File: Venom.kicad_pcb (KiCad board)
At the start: 2 copper layers, 72 x 42 mm, 13 parts, among them CN1 HC-XH-5A-G, CN2 HC-PH-8A-G, CN3 HC-XH-8A-G, CN4 HC-XH-8A-G, CN5 HC-XH-2A-G, CN6 HC-PH-7A-G, U1 Pico

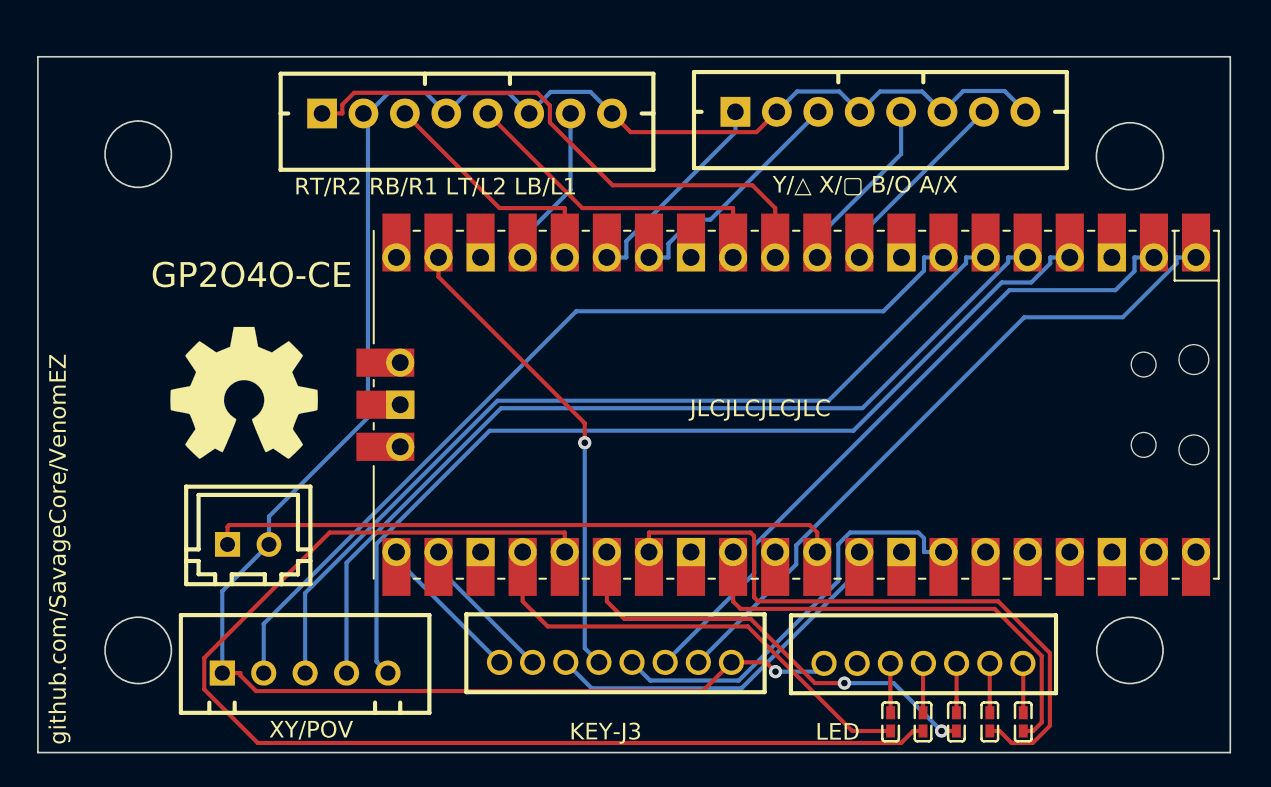
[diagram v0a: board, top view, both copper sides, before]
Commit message: Add ground fill
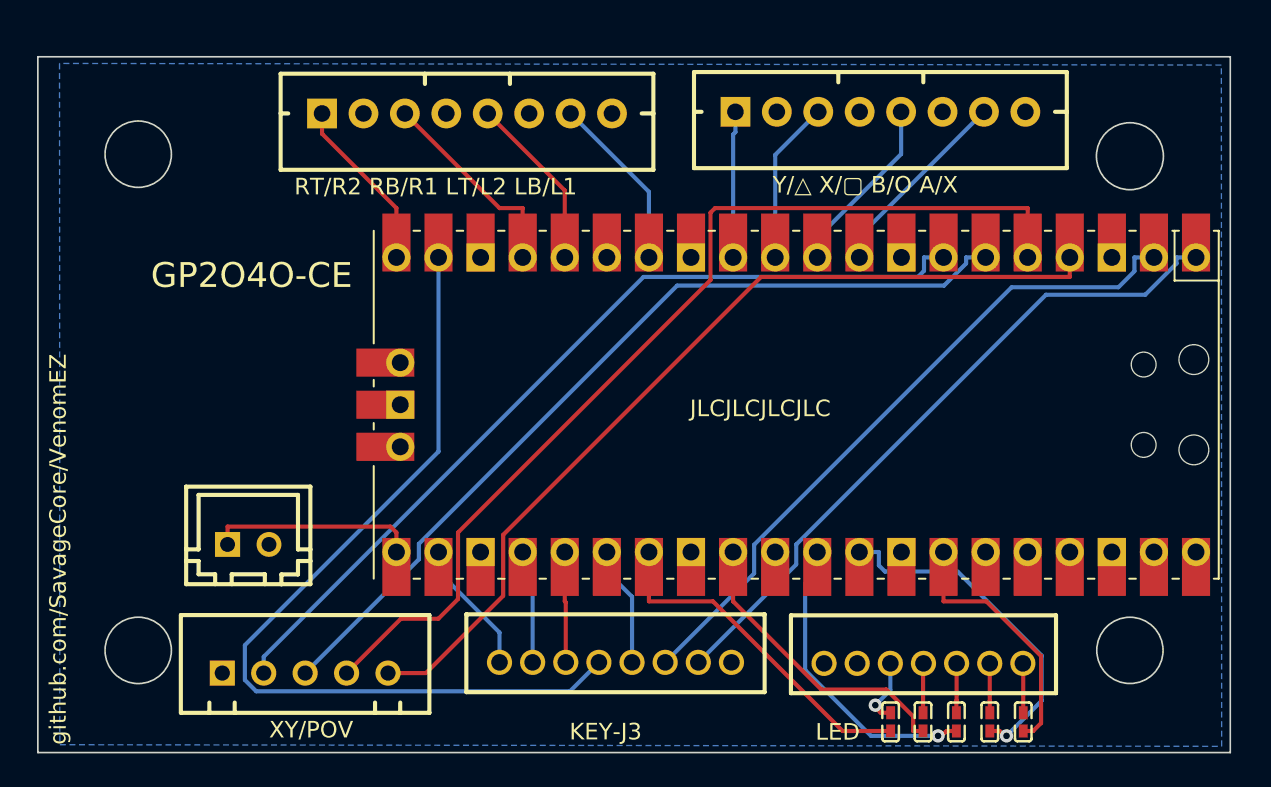
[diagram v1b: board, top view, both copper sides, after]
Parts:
- removed REF**: OSHW-Symbol_8.9x8mm_SilkScreen, Symbol:OSHW-Symbol_8.9x8mm_SilkScreen
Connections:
- U1 pad 11: (3K) R2 -> (1P) B3
- U1 pad 12: (4K) L2 -> (2P) B4
- U1 pad 14: (1P) B3 -> (4P) L1
- U1 pad 15: (2P) B4 -> unconnected-(U1-GPIO11-Pad15)
- U1 pad 16: (3P) R1 -> (4K) L2
- U1 pad 17: (4P) L1 -> (3P) R1
- U1 pad 20: unconnected-(U1-GPIO15-Pad20) -> (3K) R2
- U1 pad 21: S2 (START) -> A1 (HOME)
- U1 pad 22: S1 (SELECT) -> S2 (START)
- U1 pad 24: TLEDC1 -> S1 (SELECT)
- U1 pad 25: PLEDC4 -> A2 (TP/CAPTURE)
- U1 pad 26: PLEDC3 -> LS TOGGLE
- U1 pad 27: PLEDC2 -> TLEDC1
- U1 pad 29: PLEDC1 -> PLEDC4
- U1 pad 31: A1 (HOME) -> PLEDC3
- U1 pad 32: A2 (TP/CAPTURE) -> PLEDC2
- U1 pad 34: LS TOGGLE -> PLEDC1
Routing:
- net GND: track 124.4 -> 0.00 mm, vias 1 -> 0
- net PLEDC4: track 73.0 -> 18.2 mm
- net A1 (HOME): track 38.1 -> 12.6 mm
- net TURBO: track 28.4 -> 52.7 mm, vias 1 -> 0
- net (3K) R2: track 34.6 -> 10.6 mm
- net PLEDC2: track 39.3 -> 20.9 mm, vias 0 -> 1
- net LS TOGGLE: track 25.2 -> 7.29 mm
- net A2 (TP/CAPTURE): track 22.5 -> 6.68 mm
- net PLEDC1: track 28.3 -> 15.6 mm
- net (4K) L2: track 20.2 -> 10.6 mm
- net PLEDC3: track 27.3 -> 18.3 mm, vias 2 -> 1
- net TLEDC1: track 28.4 -> 20.8 mm
- net DOWN: track 55.6 -> 60.4 mm
- net (1P) B3: track 14.3 -> 9.87 mm
- net (2P) B4: track 12.7 -> 8.85 mm
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- added copper zone on B.Cu, net GND

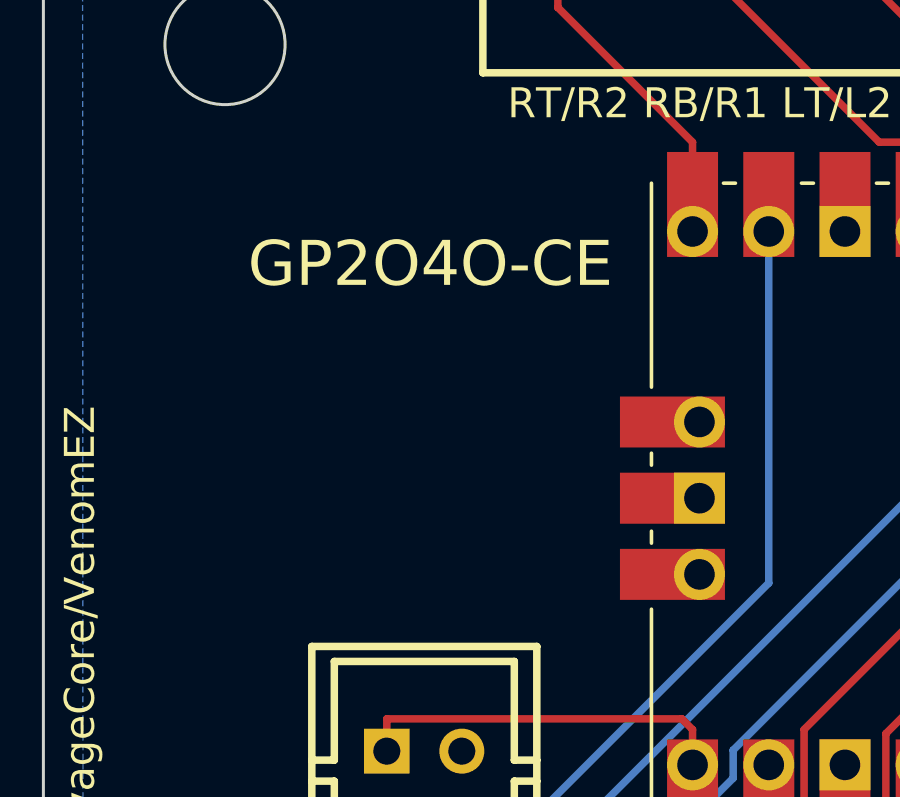
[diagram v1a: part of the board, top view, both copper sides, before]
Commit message: Add logos
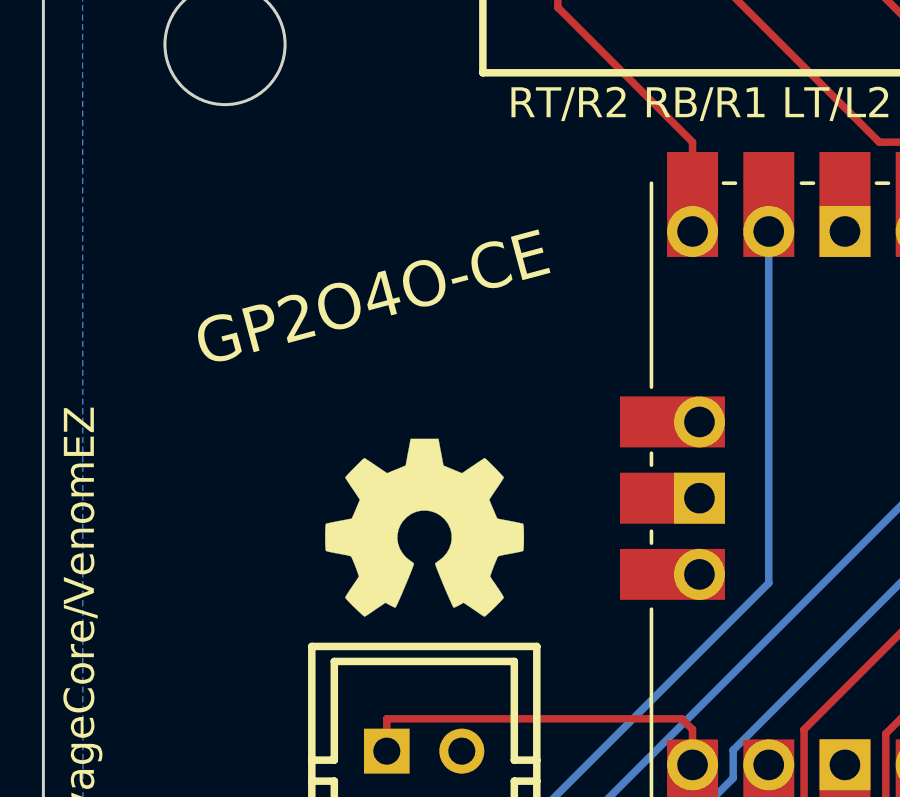
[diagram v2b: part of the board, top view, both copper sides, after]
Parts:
- added REF**: OSHW-Symbol_6.7x6mm_SilkScreen, Symbol:OSHW-Symbol_6.7x6mm_SilkScreen, F.Cu at (90.2, 96.7)

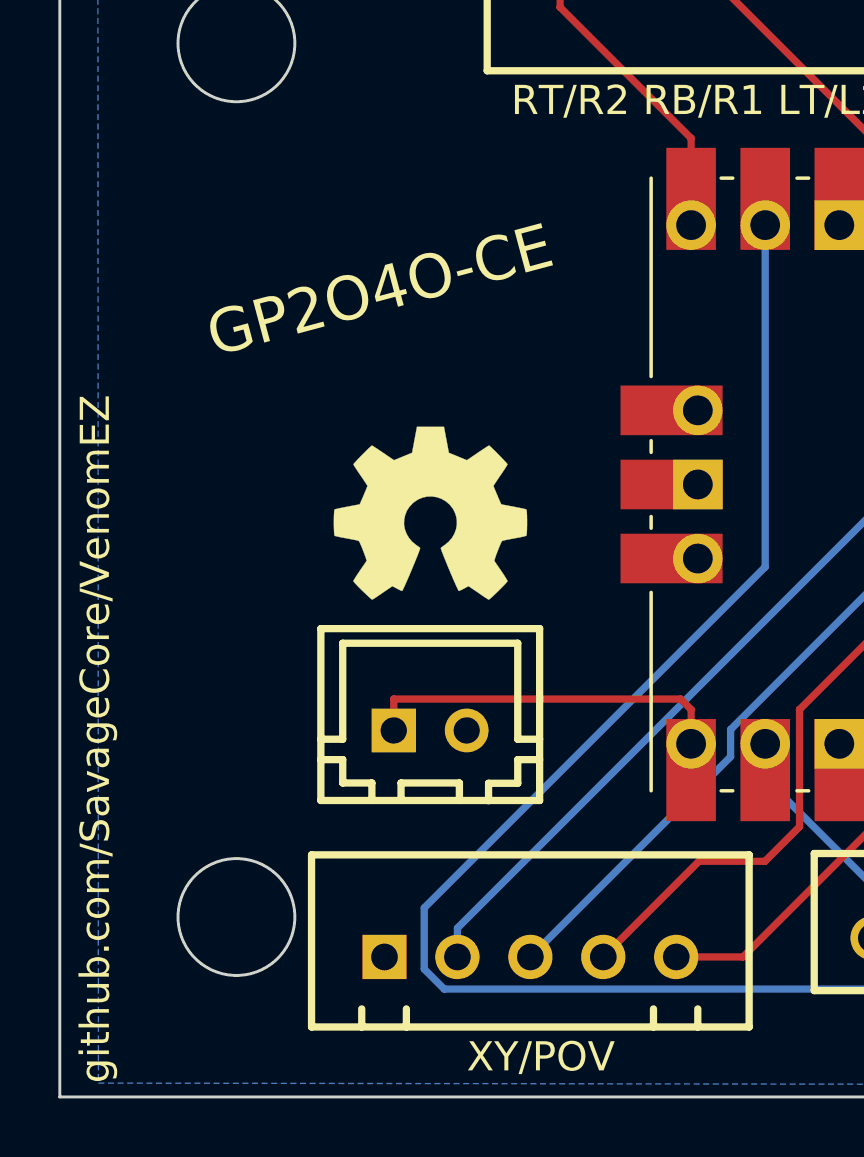
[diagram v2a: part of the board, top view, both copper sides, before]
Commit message: Add version to silk, move github link to back of board
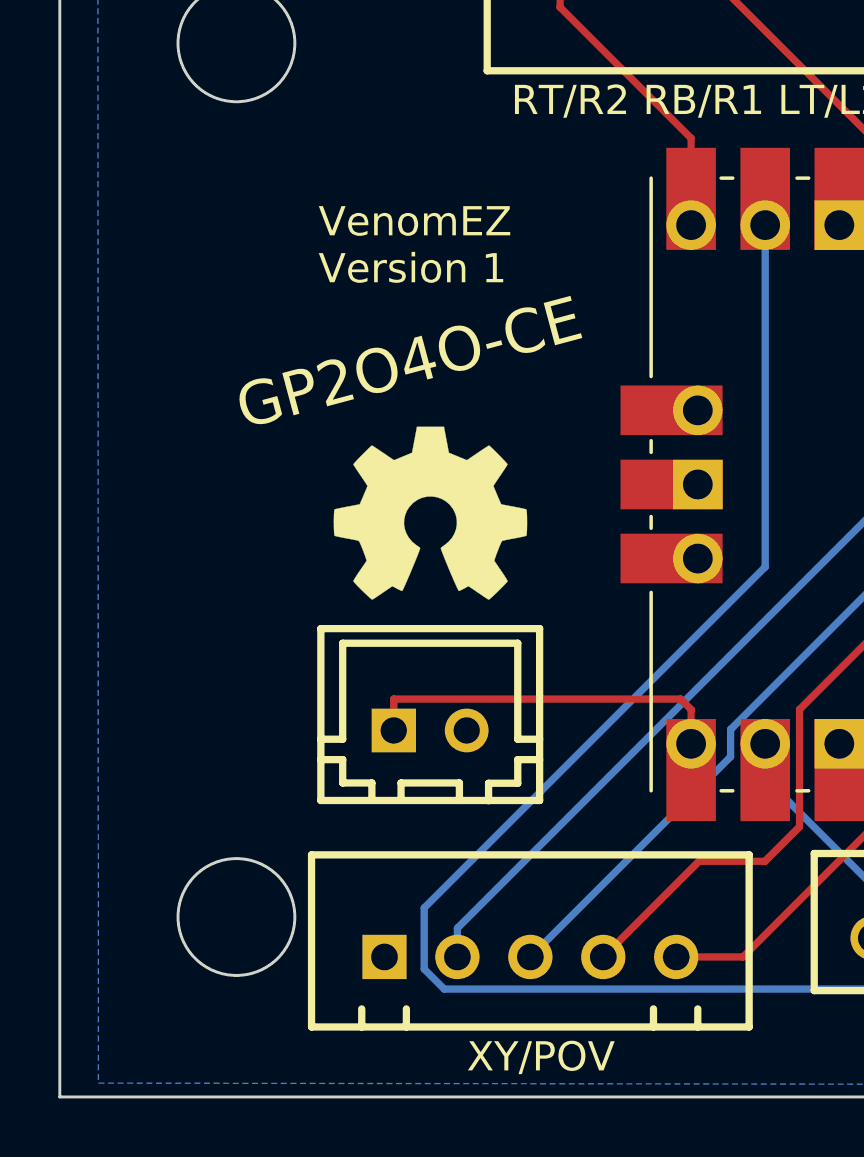
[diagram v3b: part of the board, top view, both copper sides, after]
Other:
- board text added: "VenomEZ Version 1"

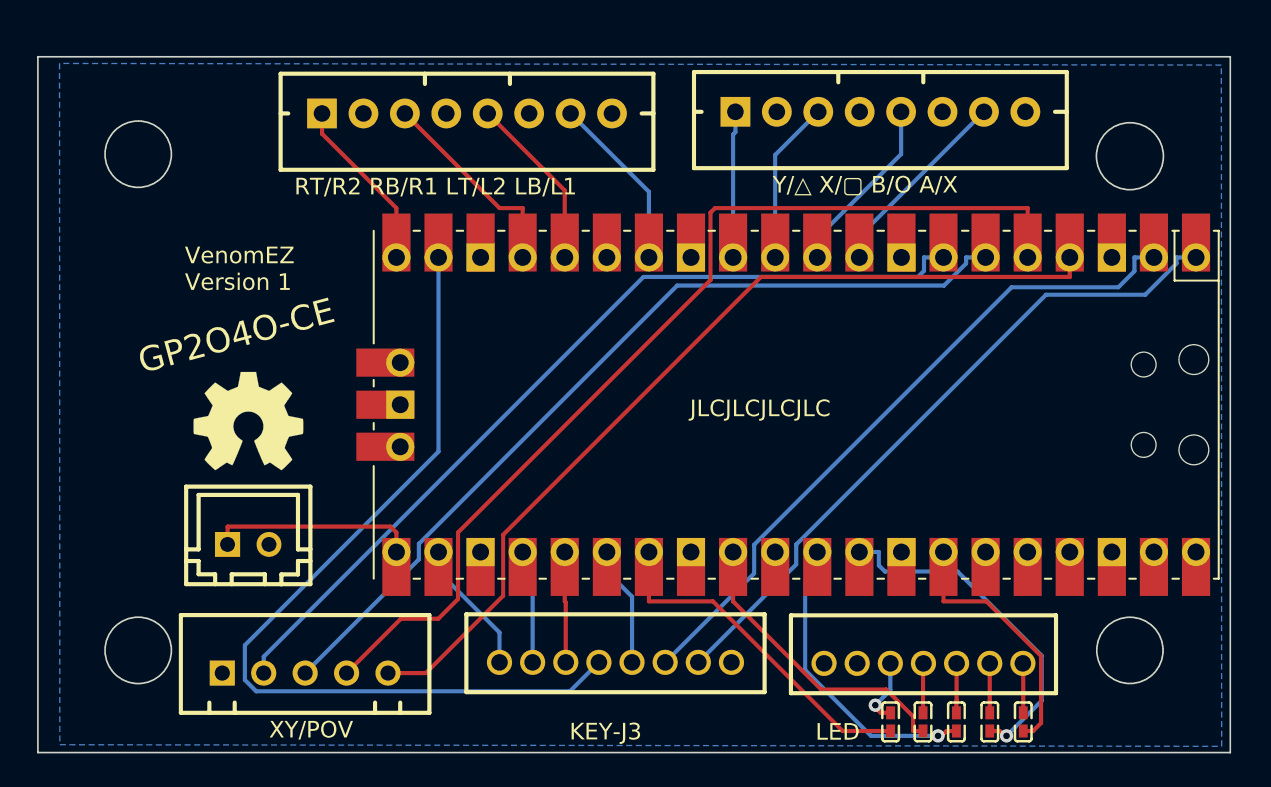
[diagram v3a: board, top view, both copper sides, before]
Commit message: Add WEB button
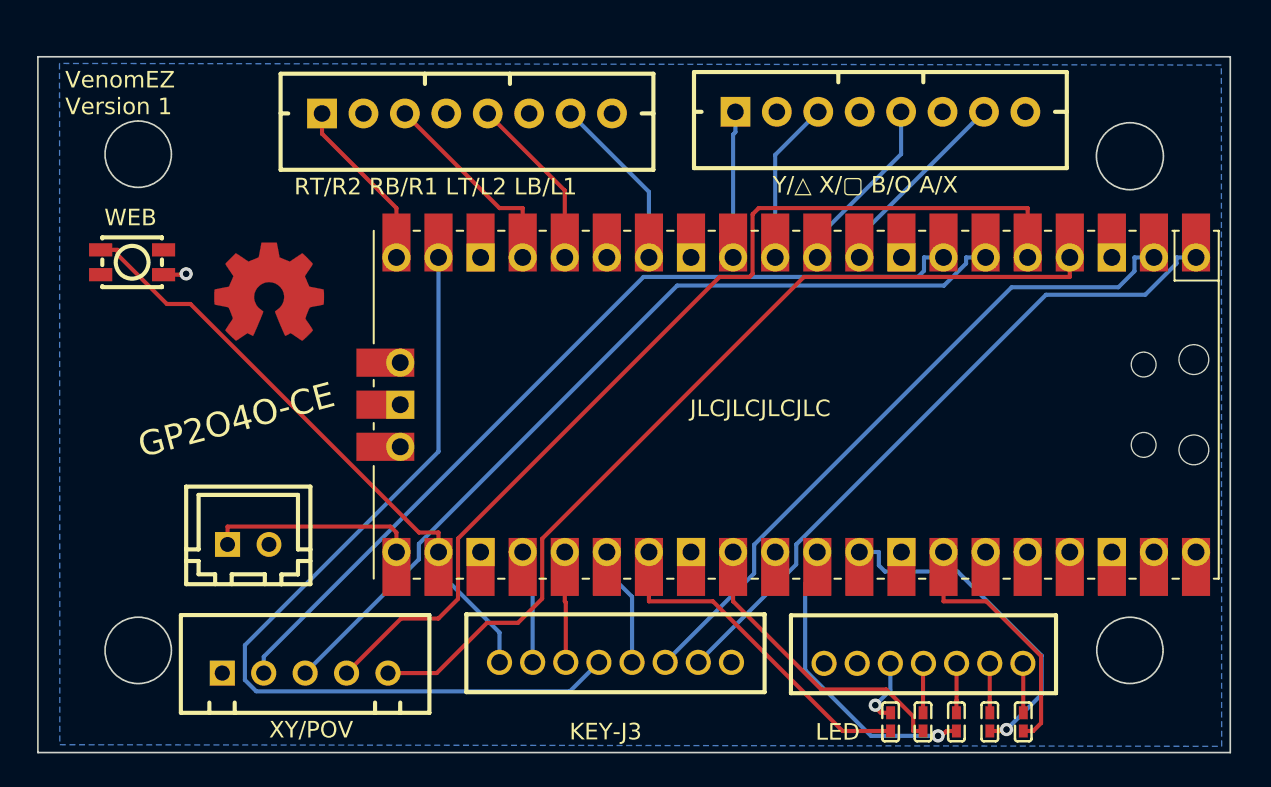
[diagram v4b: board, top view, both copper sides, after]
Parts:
- removed the REF** at (90.2, 96.7)
- added REF**: OSHW-Symbol_6.7x6mm_Copper, Symbol:OSHW-Symbol_6.7x6mm_Copper, F.Cu at (91.4, 88.9)
- added SW1: GT-TC030A-H020-L1N, easyeda2kicad:SW-SMD_4P-L3.6-W3.0-P1.50-LS4.7, F.Cu at (83.2, 87.1)
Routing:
- net S2 (START): track 8.18 -> 37.0 mm
- net GND: track 0.00 -> 1.38 mm, vias 0 -> 1
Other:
- board text added: "WEB"

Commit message: Add RESET button
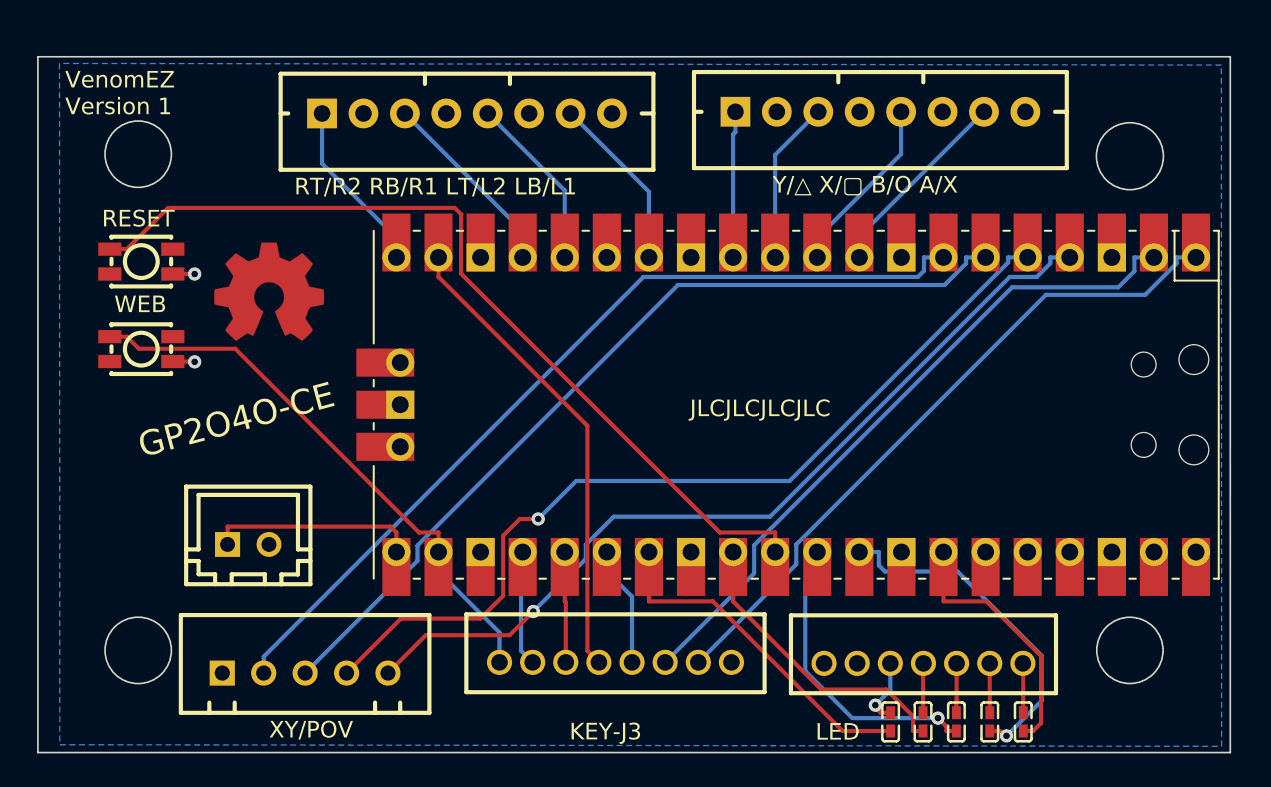
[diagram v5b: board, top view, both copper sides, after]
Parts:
- added SW2: GT-TC030A-H020-L1N, easyeda2kicad:SW-SMD_4P-L3.6-W3.0-P1.50-LS4.7, F.Cu at (83.7, 87.1)
- moved SW1 5.27 mm to (83.7, 92.4)
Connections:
- U1 pad 30: unconnected-(U1-RUN-Pad30) -> RUN
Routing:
- net RUN: track 0.00 -> 52.6 mm
- net TURBO: track 52.7 -> 28.4 mm
- net DOWN: track 59.9 -> 53.8 mm, vias 0 -> 1
- net S2 (START): track 37.0 -> 34.1 mm
- net UP: track 54.4 -> 52.3 mm, vias 0 -> 1
- net GND: track 1.38 -> 2.65 mm, vias 1 -> 2
- net (3P) R1: track 12.5 -> 11.6 mm
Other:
- board text added: "RESET"

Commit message: LEDs need a resistor not capacitor?
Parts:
- removed C1, C2, C3, C4, C5: CL05B103KB5NNNC, easyeda2kicad:C0402
- added R1: 0603WAF3300T5E, easyeda2kicad:R0603, F.Cu at (138.7, 115.0)
- added R2: 0603WAF3300T5E, easyeda2kicad:R0603, F.Cu at (136.8, 115.0)
- added R3: 0603WAF3300T5E, easyeda2kicad:R0603, F.Cu at (134.7, 115.0)
- added R4: 0603WAF3300T5E, easyeda2kicad:R0603, F.Cu at (132.7, 115.0)
- added R5: 0603WAF3300T5E, easyeda2kicad:R0603, F.Cu at (130.7, 115.0)
- moved CN6 1.80 mm to (132.7, 111.4)
- moved CN2 0.64 mm to (113.0, 111.4)
- moved CN5 0.24 mm to (90.0, 104.0), turned to 180 degrees
- moved CN1 0.22 mm to (93.8, 112.0)
- renumbered REF** to OSHW1
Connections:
- U1 pad 27: TLEDC1 -> TLEDR1
- U1 pad 29: PLEDC4 -> PLEDR4
- U1 pad 31: PLEDC3 -> PLEDR3
- U1 pad 32: PLEDC2 -> PLEDR2
- U1 pad 34: PLEDC1 -> PLEDR1
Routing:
- net PLEDR1: track 0.00 -> 28.0 mm
- net PLEDR2: track 0.00 -> 24.8 mm
- net TLEDR1: track 0.00 -> 22.7 mm
- net PLEDC2: track 20.9 -> 0.00 mm, vias 1 -> 0
- net TLEDC1: track 20.8 -> 0.00 mm
- net PLEDR4: track 0.00 -> 20.1 mm
- net PLEDR3: track 0.00 -> 20.0 mm, vias 0 -> 1
- net PLEDC3: track 18.3 -> 0.00 mm, vias 1 -> 0
- net PLEDC4: track 18.2 -> 0.00 mm
- net PLEDC1: track 15.6 -> 0.00 mm
- net A1 (HOME): track 12.6 -> 9.30 mm
- net DOWN: track 53.8 -> 52.5 mm, vias 1 -> 0
- net TURBO LED: track 4.09 -> 2.88 mm, vias 1 -> 0
- net UP: track 52.3 -> 52.4 mm, vias 1 -> 0

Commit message: Change silk
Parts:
- moved OSHW1 9.07 mm to (89.9, 97.8)
- moved SW2 2.58 mm to (81.2, 87.4)
- moved SW1 2.57 mm to (81.2, 92.6)
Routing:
- net RUN: track 52.6 -> 92.7 mm
- net TURBO: track 28.8 -> 53.1 mm
- net GND: track 2.74 -> 6.32 mm, vias 2 -> 3
- net S2 (START): track 34.5 -> 36.9 mm
- net UP: track 52.4 -> 54.3 mm
- net RIGHT: track 52.2 -> 54.1 mm
- net DOWN: track 52.5 -> 53.7 mm
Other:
- board text added: "Revision 1"
- board text added: "VenomEZ"
- board text removed: "VenomEZ Version 1"
